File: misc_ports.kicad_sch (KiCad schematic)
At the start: 13 parts

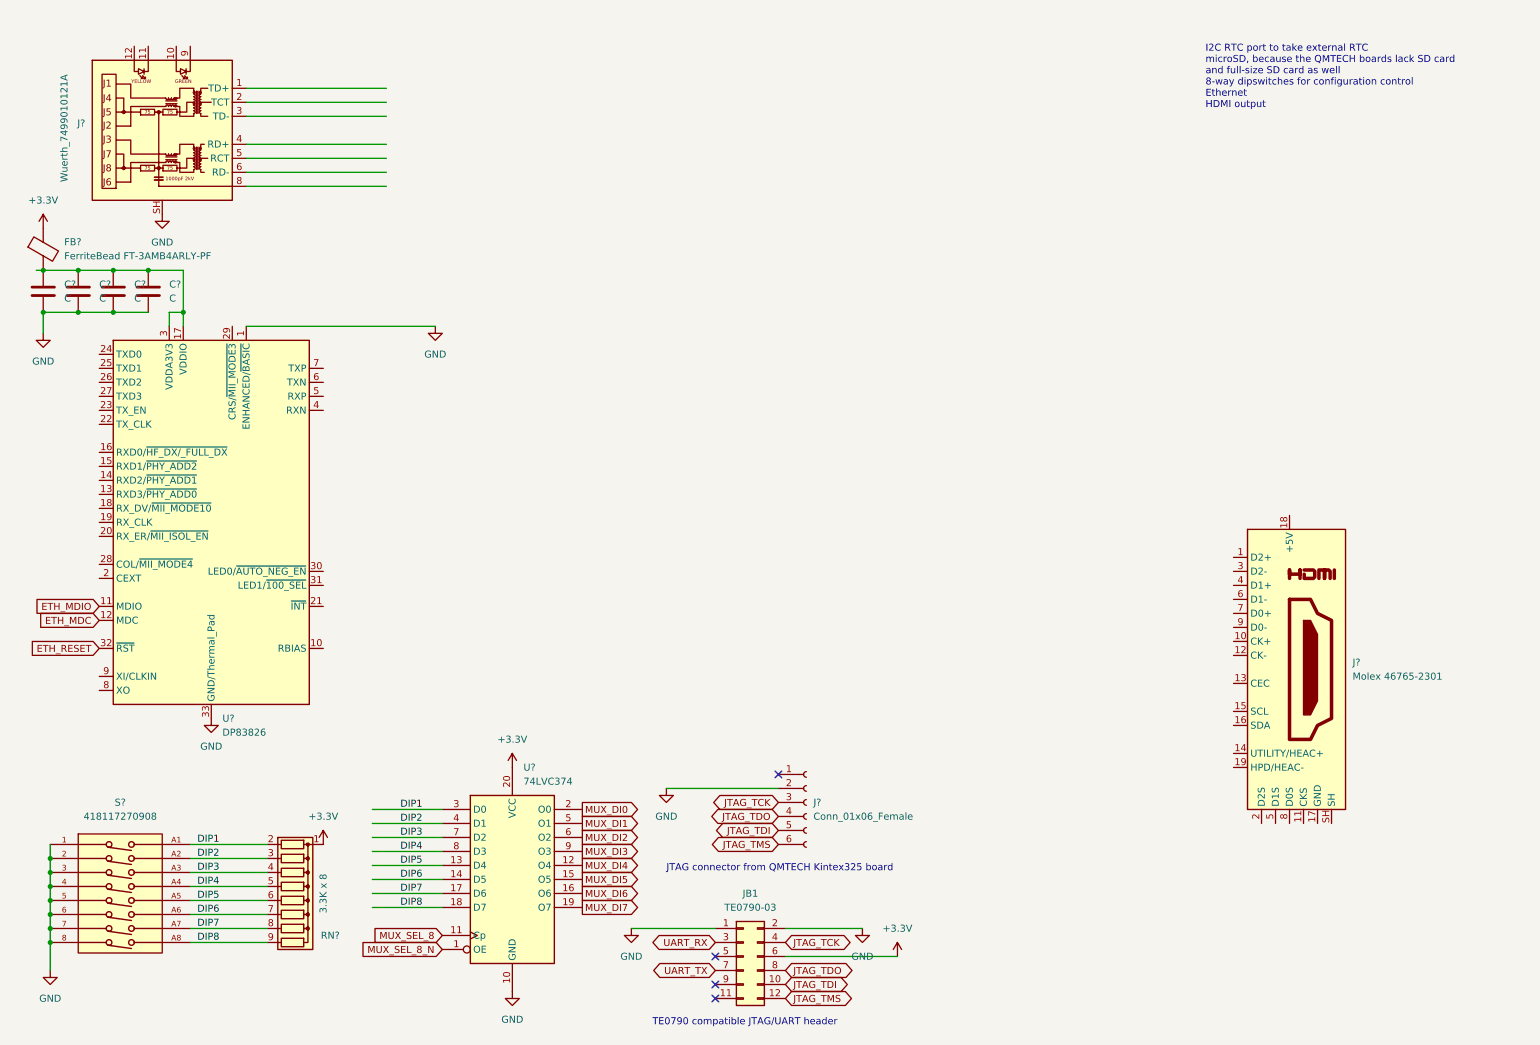
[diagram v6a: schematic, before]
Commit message: work on digital video output
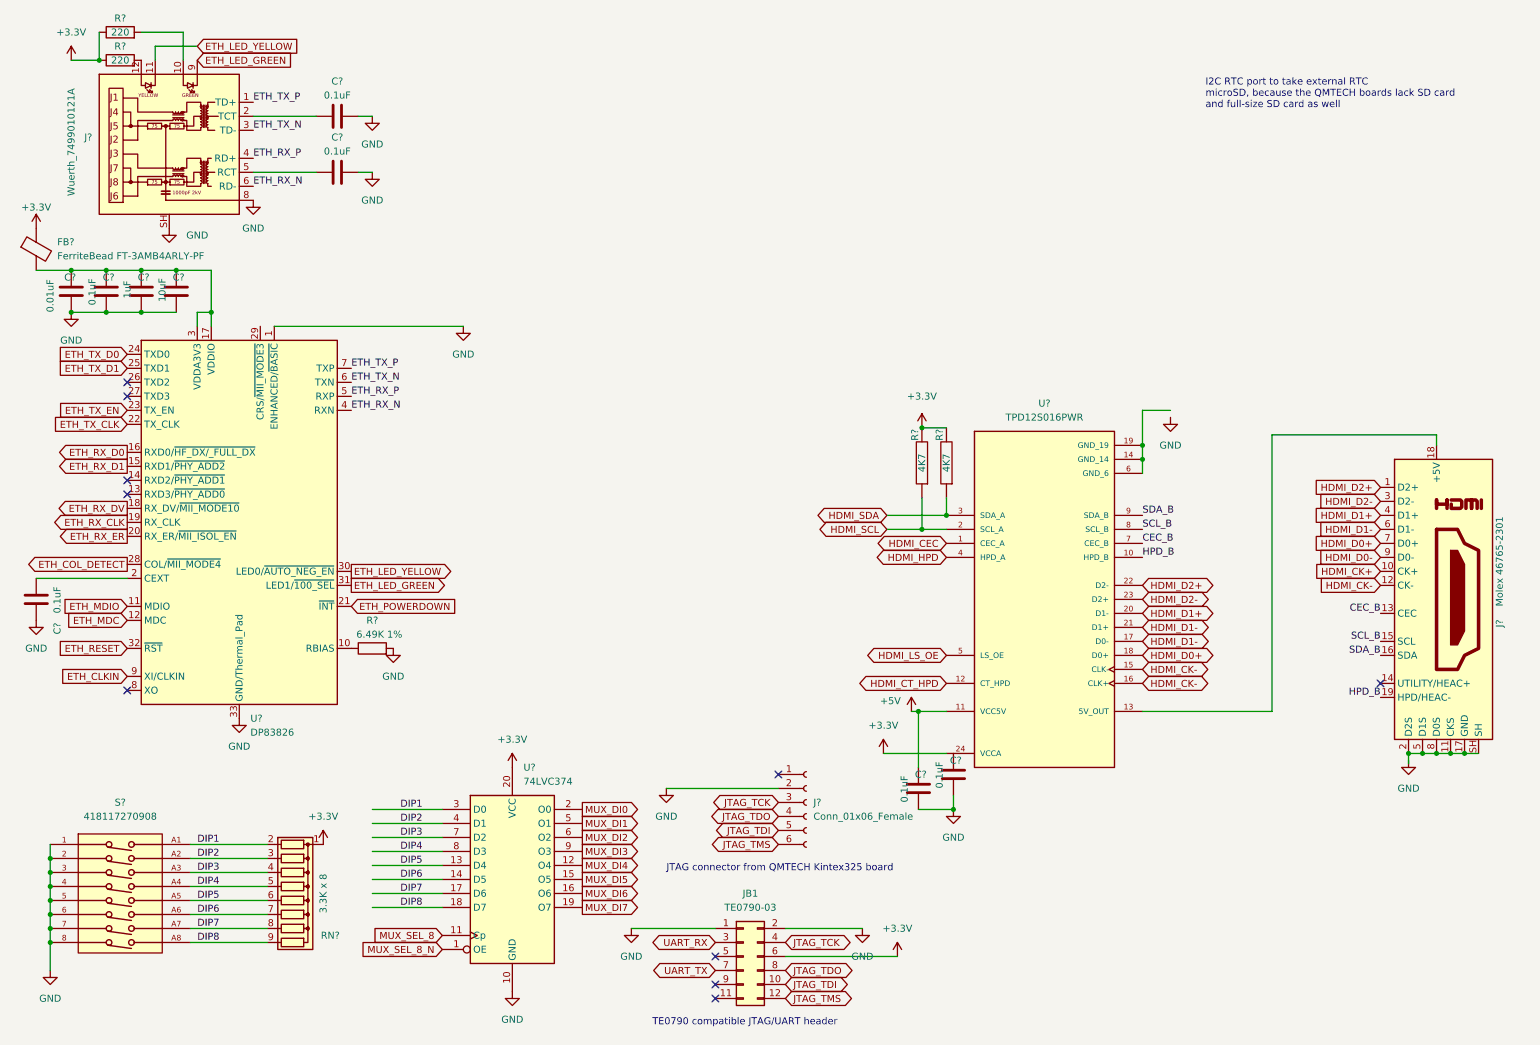
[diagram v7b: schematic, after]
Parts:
- added C? (x5): 0.1uF, symbol Device:C
- added R? (x2): 220, Resistor_THT:R_Axial_DIN0204_L3.6mm_D1.6mm_P7.62mm_Horizontal, symbol Device:R
- added R? (x2): 4K7, Resistor_THT:R_Box_L8.4mm_W2.5mm_P5.08mm, symbol pspice:R
- added R?: 6.49K 1%, Resistor_THT:R_Axial_DIN0204_L3.6mm_D1.6mm_P7.62mm_Horizontal, symbol Device:R
- added U?: TPD12S016PWR, SOP65P640X120-24N, symbol 00Project-HDMI-Helper:TPD12S016PWR
- C?: value C -> 0.1uF
- C?: value C -> 1uF
- C?: value C -> 0.01uF
- C?: value C -> 10uF
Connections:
- net +3V3: now also R?.1, R?.1, R?.2, R?.2, U?.24 (VCCA)
- net GND: now also J?.8, C?.2, C?.2, C?.2, C?.2, C?.2, R?.2
- net at U?.10 (RBIAS): now also R?.1
- net ETH_RX_D1: now reaches U?.15 (RXD1/~{PHY_ADD2})
- net ETH_RX_D0: now reaches U?.16 (RXD0/~{HF_DX/_FULL_DX})
- net ETH_RX_DV: now reaches U?.18 (RX_DV/~{MII_MODE10})
- net ETH_RX_CLK: now reaches U?.19 (RX_CLK)
- net at U?.2 (CEXT): now also C?.1
- net ETH_RX_ER: now reaches U?.20 (RX_ER/~{MII_ISOL_EN})
- net ETH_POWERDOWN: now reaches U?.21 (~{INT})
- net ETH_TX_CLK: now reaches U?.22 (TX_CLK)
- net ETH_TX_EN: now reaches U?.23 (TX_EN)
- net ETH_TX_D0: now reaches U?.24 (TXD0)
- net ETH_TX_D1: now reaches U?.25 (TXD1)
- net ETH_COL_DETECT: now reaches U?.28 (COL/~{MII_MODE4})
- net ETH_LED_YELLOW: now reaches U?.30 (LED0/~{AUTO_NEG_EN})
- net ETH_LED_YELLOW: now also J?.11
- net ETH_LED_GREEN: now reaches U?.31 (LED1/~{100_SEL})
- net ETH_LED_GREEN: now also J?.9
- net ETH_RX_N: now reaches U?.4 (RXN)
- net ETH_RX_N: now also J?.6 (RD-)
- net ETH_RX_P: now reaches U?.5 (RXP)
- net ETH_RX_P: now also J?.4 (RD+)
- net ETH_TX_N: now reaches U?.6 (TXN)
- net ETH_TX_N: now also J?.3 (TD-)
- net ETH_TX_P: now reaches U?.7 (TXP)
- net ETH_TX_P: now also J?.1 (TD+)
- net ETH_CLKIN: now reaches U?.9 (XI/CLKIN)
- net HDMI_D2+: now reaches J?.1 (D2+)
- net HDMI_D2+: now also U?.22 (D2-)
- net HDMI_CK+: now reaches J?.10 (CK+)
- net at J?.11 (CKS): now also J?.17 (GND), J?.2 (D2S), J?.5 (D1S), J?.8 (D0S), J?.SH
- net HDMI_CK-: now reaches J?.12 (CK-)
- net HDMI_CK-: now also U?.15 (CLK-), U?.16 (CLK+)
- net CEC_B: now reaches J?.13 (CEC)
- net CEC_B: now also U?.7 (CEC_B)
- net SCL_B: now reaches J?.15 (SCL)
- net SCL_B: now also U?.8 (SCL_B)
- net SDA_B: now reaches J?.16 (SDA)
- net SDA_B: now also U?.9 (SDA_B)
- net at J?.18 (+5V): now also U?.13 (5V_OUT)
- net HPD_B: now reaches J?.19 (HPD/HEAC-)
- net HPD_B: now also U?.10 (HPD_B)
- net HDMI_D2-: now reaches J?.3 (D2-)
- net HDMI_D2-: now also U?.23 (D2+)
- net HDMI_D1+: now reaches J?.4 (D1+)
- net HDMI_D1+: now also U?.20 (D1-)
- net HDMI_D1-: now reaches J?.6 (D1-)
- net HDMI_D1-: now also U?.17 (D0-), U?.21 (D1+)
- net HDMI_D0+: now reaches J?.7 (D0+)
- net HDMI_D0+: now also U?.18 (D0+)
- net HDMI_D0-: now reaches J?.9 (D0-)
- net at J?.10: now also R?.2
- net at J?.12: now also R?.2
- net at J?.2 (TCT): now also C?.1
- net at J?.5 (RCT): now also C?.1
- new net: U?.14 (GND_14), U?.19 (GND_19), U?.6 (GND_6)
- new net +5V: C?.1, U?.11 (VCC5V)
- new net HDMI_CEC: U?.1 (CEC_A)
- new net HDMI_CT_HPD: U?.12 (CT_HPD)
- new net HDMI_HPD: U?.4 (HPD_A)
- new net HDMI_LS_OE: U?.5 (LS_OE)
- new net HDMI_SCL: R?.1, U?.2 (SCL_A)
- new net HDMI_SDA: R?.1, U?.3 (SDA_A)
- no-connect marks 4 -> 10
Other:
- note added: "I2C RTC port to take external RTC microSD, because the QMTECH boards lack SD card and full-size SD card as well"
- note removed: "I2C RTC port to take external RTC microSD, because the QMTECH boards lack SD card and full-size SD card as well 8-way dipswitches for configuration control Ethernet HDMI output"
- moved on the sheet: C?, FB?, J?, U?

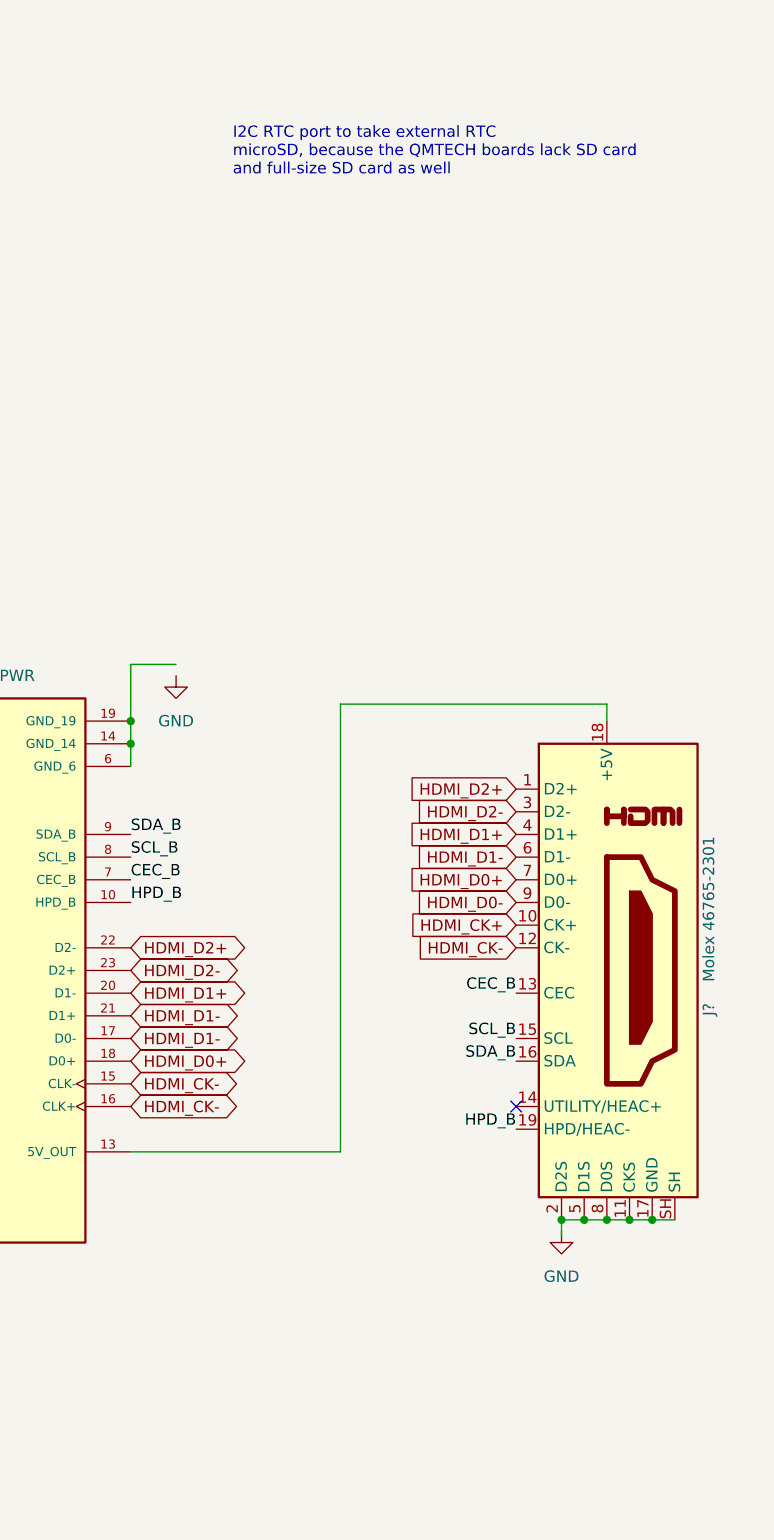
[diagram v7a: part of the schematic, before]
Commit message: add RTC I2C header
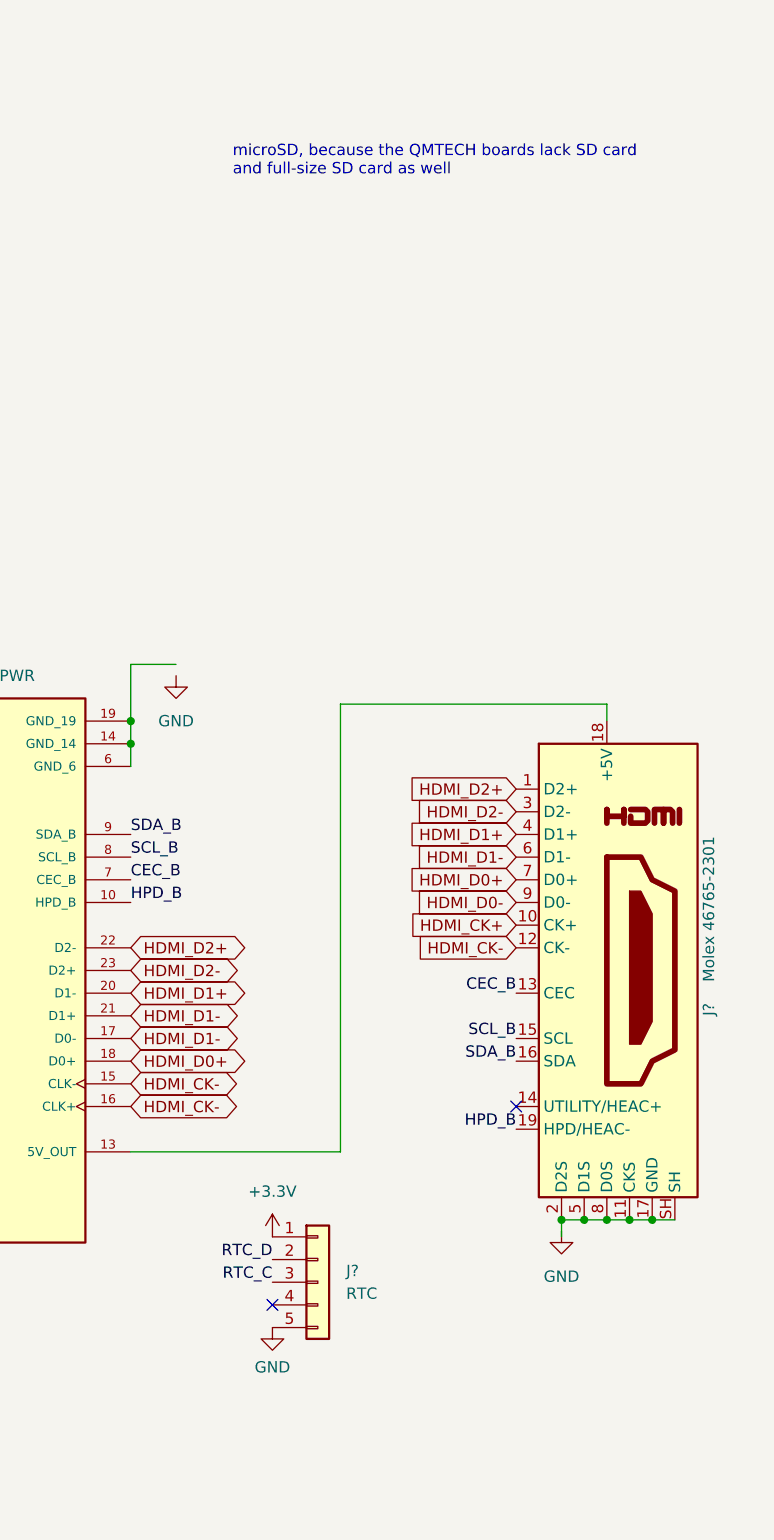
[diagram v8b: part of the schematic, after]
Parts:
- added J?: RTC, Connector_PinHeader_2.54mm:PinHeader_1x05_P2.54mm_Vertical, symbol Connector_Generic:Conn_01x05
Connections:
- net +3V3: now also J?.1 (Pin_1)
- net GND: now also J?.5 (Pin_5)
- new net RTC_C: J?.3 (Pin_3)
- new net RTC_D: J?.2 (Pin_2)
- no-connect marks 10 -> 11
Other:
- note added: "microSD, because the QMTECH boards lack SD card and full-size SD card as well"
- note removed: "I2C RTC port to take external RTC microSD, because the QMTECH boards lack SD card and full-size SD card as well"
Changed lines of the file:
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@@
   (no_connect (at 138.43 189.23))
   (no_connect (at 138.43 184.15))
+  (no_connect (at 231.775 156.845))
   (no_connect (at 31.75 100.33))
   (no_connect (at 31.75 97.79))
@@
     (effects (font (size 1.27 1.27)) (justify left bottom))
   )
-  (text "I2C RTC port to take external RTC\nmicroSD, because the QMTECH boards lack SD card\nand full-size SD card as well"
+  (text "microSD, because the QMTECH boards lack SD card\nand full-size SD card as well"
     (at 227.33 30.48 0)
     (effects (font (size 1.27 1.27)) (justify left bottom))
@@
     (effects (font (size 1.27 1.27)) (justify left bottom))
   )
+  (label "RTC_D" (at 231.775 151.765 180)
+    (effects (font (size 1.27 1.27)) (justify right bottom))
+  )
   (label "SCL_B" (at 259.08 127 180)
     (effects (font (size 1.27 1.27)) (justify right bottom))
@@
   (label "DIP3" (at 44.45 168.91 0)
     (effects (font (size 1.27 1.27)) (justify left bottom))
+  )
+  (label "RTC_C" (at 231.775 154.305 180)
+    (effects (font (size 1.27 1.27)) (justify right bottom))
   )
   (label "DIP7" (at 44.45 179.07 0)
@@
     (pin "1")
     (pin "2")
+  )
+  (symbol (lib_id "power:GND") (at 231.775 159.385 0) (unit 1)
+    (in_bom yes) (on_board yes) (fields_autoplaced)
+    (property "Reference" "#PWR?" (id 0) (at 231.775 165.735 0)
+      (effects (font (size 1.27 1.27)) hide)
+    )
+    (property "Value" "GND" (id 1) (at 231.775 163.83 0))
+    (property "Footprint" "" (id 2) (at 231.775 159.385 0)
+      (effects (font (size 1.27 1.27)) hide)
+    )
+    (property "Datasheet" "" (id 3) (at 231.775 159.385 0)
+      (effects (font (size 1.27 1.27)) hide)
+    )
+    (pin "1")
   )
   (symbol (lib_id "Device:R_Network08") (at 62.23 173.99 270) (unit 1)
@@
     (pin "1")
   )
+  (symbol (lib_id "Connector_Generic:Conn_01x05") (at 236.855 154.305 0) (unit 1)
+    (in_bom yes) (on_board yes) (fields_autoplaced)
+    (property "Reference" "J?" (id 0) (at 240.03 153.0349 0)
+      (effects (font (size 1.27 1.27)) (justify left))
+    )
+    (property "Value" "RTC" (id 1) (at 240.03 155.5749 0)
+      (effects (font (size 1.27 1.27)) (justify left))
+    )
+    (property "Footprint" "Connector_PinHeader_2.54mm:PinHeader_1x05_P2.54mm_Vertical" (id 2) (at 236.855 154.305 0)
+      (effects (font (size 1.27 1.27)) hide)
+    )
+    (property "Datasheet" "~" (id 3) (at 236.855 154.305 0)
+      (effects (font (size 1.27 1.27)) hide)
+    )
+    (pin "1")
+    (pin "2")
+    (pin "3")
+    (pin "4")
+    (pin "5")
+  )
   (symbol (lib_id "Device:C") (at 69.85 41.91 90) (unit 1)
     (in_bom yes) (on_board yes)
@@
     (pin "2")
   )
+  (symbol (lib_id "power:+3.3V") (at 231.775 149.225 0) (unit 1)
+    (in_bom yes) (on_board yes) (fields_autoplaced)
+    (property "Reference" "#PWR?" (id 0) (at 231.775 153.035 0)
+      (effects (font (size 1.27 1.27)) hide)
+    )
+    (property "Value" "+3.3V" (id 1) (at 231.775 144.145 0))
+    (property "Footprint" "" (id 2) (at 231.775 149.225 0)
+      (effects (font (size 1.27 1.27)) hide)
+    )
+    (property "Datasheet" "" (id 3) (at 231.775 149.225 0)
+      (effects (font (size 1.27 1.27)) hide)
+    )
+    (pin "1")
+  )
   (symbol (lib_id "Device:R") (at 76.2 128.27 90) (unit 1)
